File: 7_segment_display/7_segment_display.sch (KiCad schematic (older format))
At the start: 15 parts, among them J1 Conn_01x05_Male, J2 Conn_01x05_Female, U1 74HC595, U2 SBC18-11SURKCGKWA

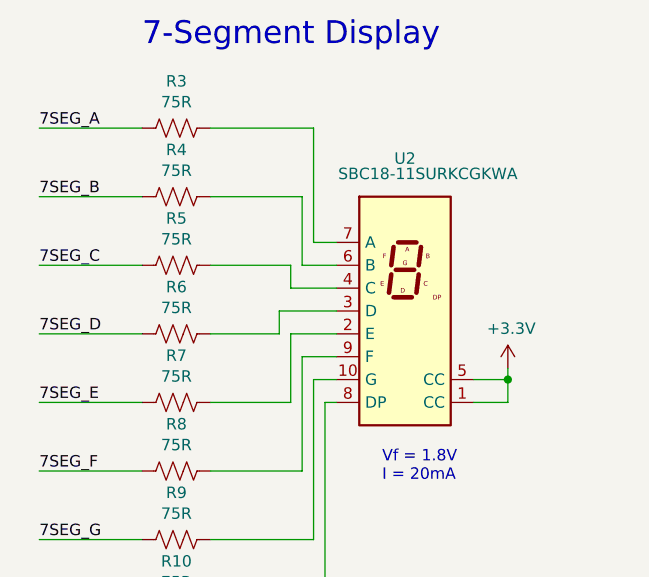
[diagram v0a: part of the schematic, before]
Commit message: Make one that actually works
Use correct pin footprint for 7 segment display
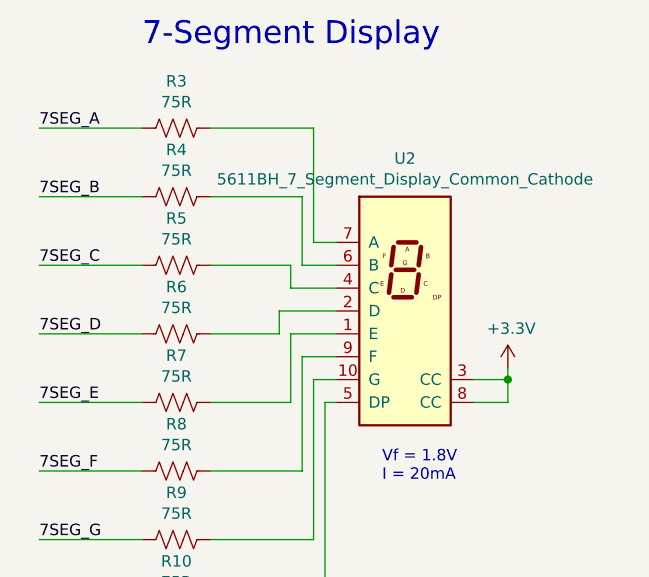
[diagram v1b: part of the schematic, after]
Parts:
- removed U2: SBC18-11SURKCGKWA, lib_fp:5611BH, symbol Display_Character:SBC18-11SURKCGKWA
- added U2: 5611BH_7_Segment_Display_Common_Cathode, lib_fp:5611BH, symbol lib_sch:5611BH_7_Segment_Display_Common_Cathode
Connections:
- net +3V3: now also U2.3 (CC), U2.8 (CC)
- net at R9.1: now also U2.10 (G)
- net at R7.1: now also U2.1 (E)
- net at R6.1: now also U2.2 (D)
- net at R5.1: now also U2.4 (C)
- net at R4.1: now also U2.6 (B)
- net at R3.1: now also U2.7 (A)
- net at R10.1: now also U2.5 (DP)
- net at R8.1: now also U2.9 (F)
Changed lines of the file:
@@
 EESchema Schematic File Version 4
+LIBS:7_segment_display-cache
 EELAYER 26 0
 EELAYER END
@@
 Wire Wire Line
 	2600 3300 2900 3300
-$Comp
-L Display_Character:SBC18-11SURKCGKWA U2
-U 1 1 5CD9443F
-P 7650 2500
-F 0 "U2" H 7650 3167 50  0000 C CNN
-F 1 "SBC18-11SURKCGKWA" H 7750 3100 50  0000 C CNN
-F 2 "lib_fp:5611BH" H 6920 1790 50  0001 L CNN
-F 3 "http://www.kingbright.com/attachments/file/psearch/000/00/00/SBC18-11SURKCGKWA(Ver.6A).pdf" H 7650 2690 50  0001 L CNN
-	1    7650 2500
-	1    0    0    -1
-$EndComp
 Wire Wire Line
 	3700 2800 4200 2800
@@
 Wire Wire Line
 	2000 4800 2000 4850
+$Comp
+L lib_sch:5611BH_7_Segment_Display_Common_Cathode U2
+U 1 1 5CD9E98C
+P 7650 2250
+F 0 "U2" H 7650 2667 50  0000 C CNN
+F 1 "5611BH_7_Segment_Display_Common_Cathode" H 7650 2576 50  0000 C CNN
+F 2 "lib_fp:5611BH" H 7650 2700 50  0001 C CNN
+F 3 "" H 7650 2700 50  0001 C CNN
+	1    7650 2250
+	1    0    0    -1
+$EndComp
 $EndSCHEMATC
